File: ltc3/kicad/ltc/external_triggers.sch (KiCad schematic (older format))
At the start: 40 parts, among them P601 JST PH header, P602 JST PH housing, P605 MicroFit header, P606 MicroFit recept., P607 PowerPole, P608 PowerPole, P609 PowerPole, P610 PowerPole, P611 PowerPole, P612 PowerPole, P613 PowerPole, P614 PowerPole, Q601 PMV45EN, Q602 PMV45EN, Q603 PMV45EN, Q604 PMV45EN, SW601 SP3T, SW602 SP3T, SW603 SP3T, SW604 SP3T, U601 TLP3542, U602 TLP3542, U603 TLP3542, U604 TLP3542

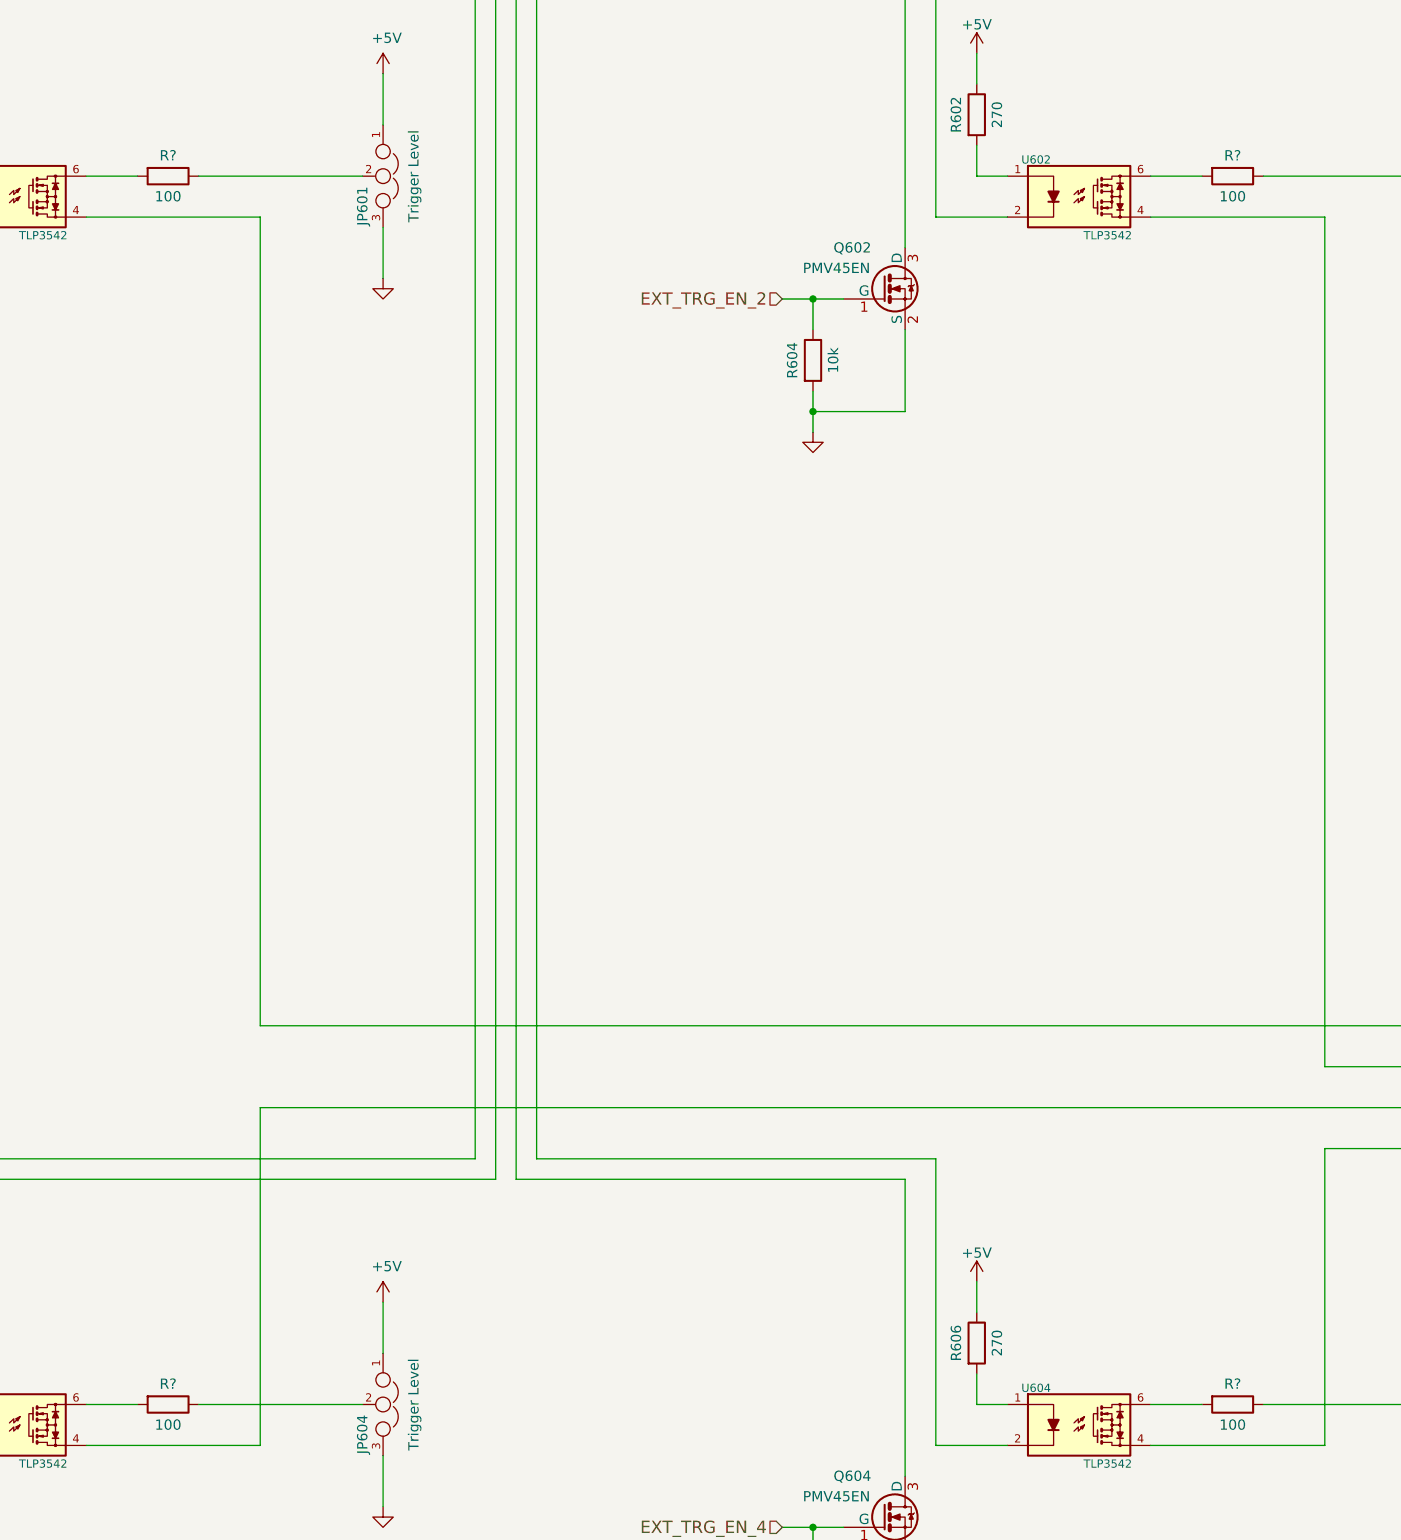
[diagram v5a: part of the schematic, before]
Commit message: LTC3: Modified LTC ignition control schematic.
Gave ignition battery ground node a distinctive symbol.
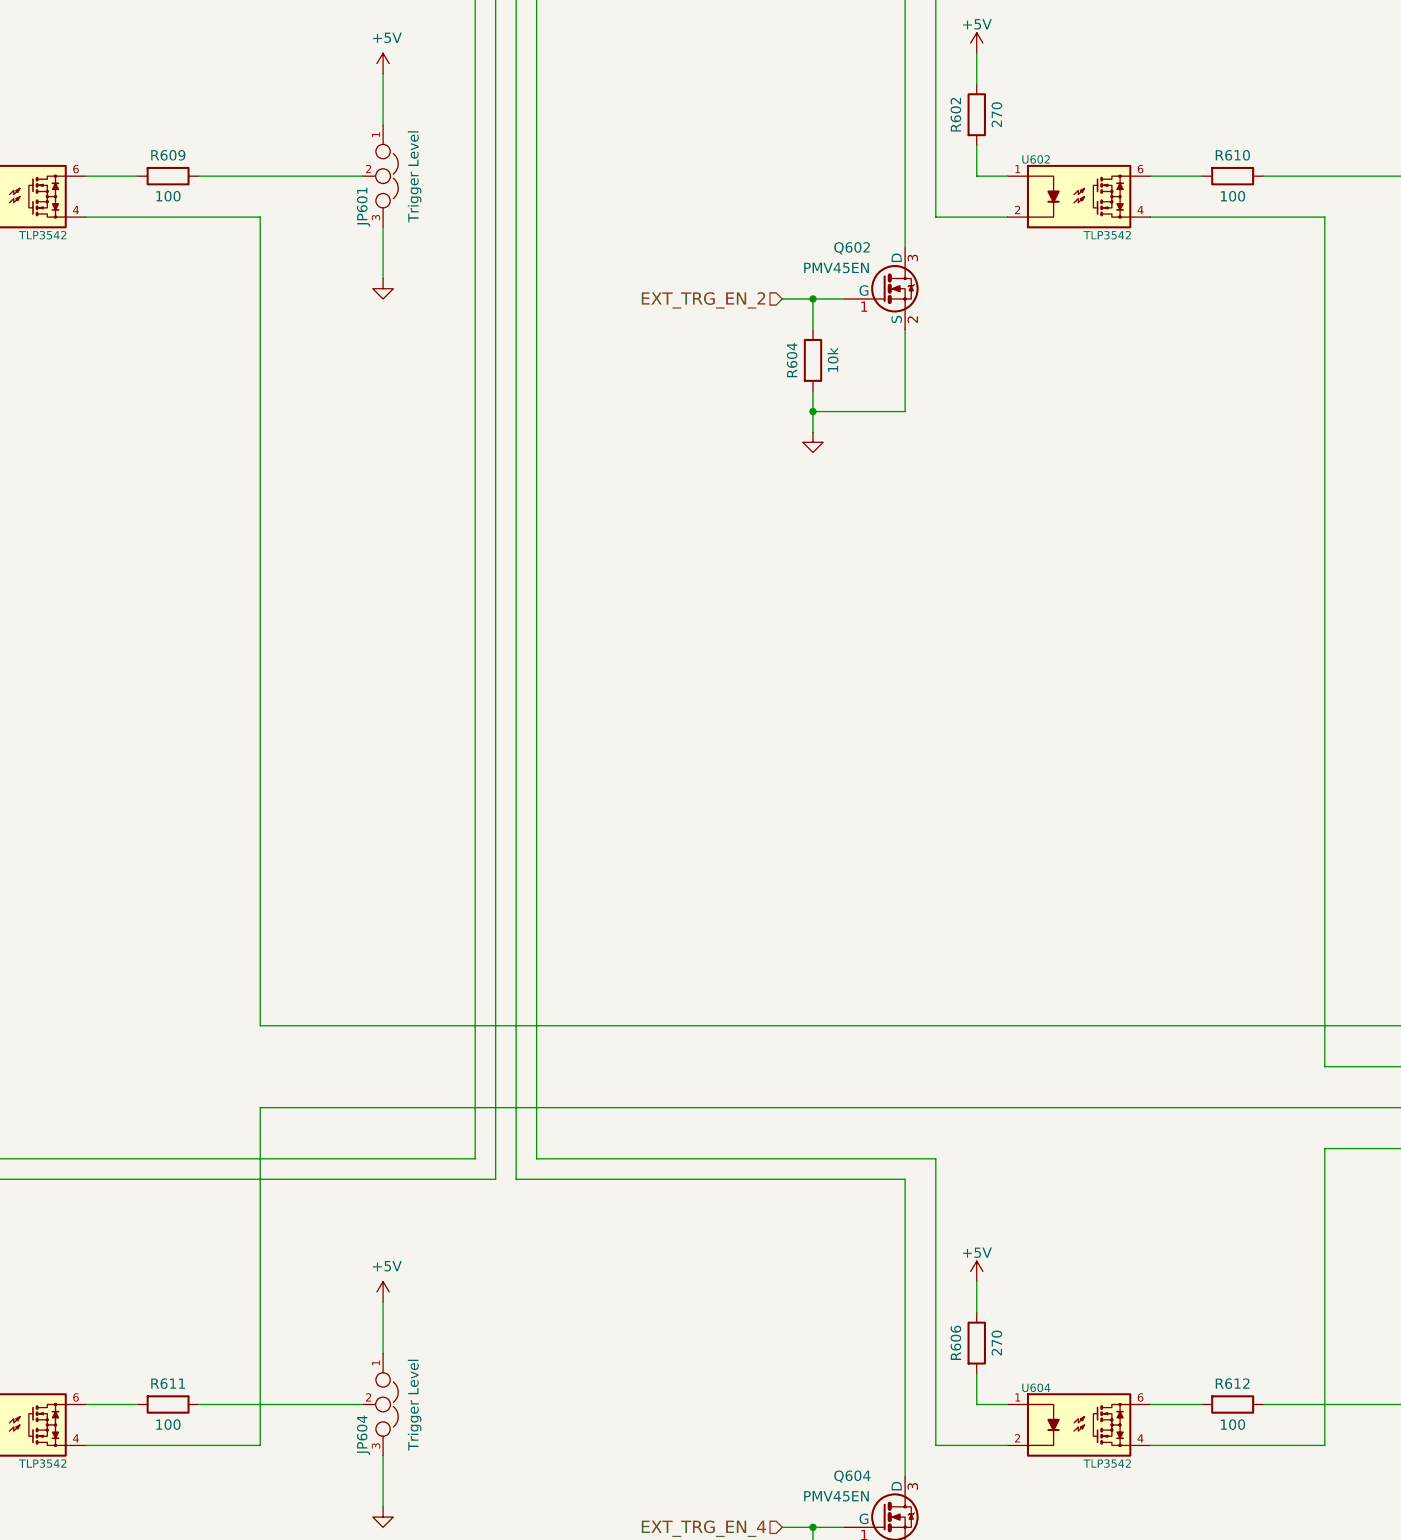
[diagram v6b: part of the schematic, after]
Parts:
- gave numbers to parts that had none: 4
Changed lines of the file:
@@
 $EndComp
 $Comp
-L GND #PWR615
+L GND #PWR616
 U 1 1 5725D3AE
 P 9850 9350
-F 0 "#PWR615" H 9850 9350 30  0001 C CNN
+F 0 "#PWR616" H 9850 9350 30  0001 C CNN
 F 1 "GND" H 9850 9280 30  0001 C CNN
 F 2 "" H 9850 9350 60  0000 C CNN
@@
 	9850 8350 9850 8600
 $Comp
-L +5V #PWR613
+L +5V #PWR614
 U 1 1 5725D3B6
 P 9850 8350
-F 0 "#PWR613" H 9850 8200 50  0001 C CNN
+F 0 "#PWR614" H 9850 8200 50  0001 C CNN
 F 1 "+5V" H 9868 8524 50  0000 C CNN
 F 2 "" H 9850 8350 50  0000 C CNN
@@
 $EndComp
 $Comp
-L GND #PWR616
+L GND #PWR615
 U 1 1 5725DD7F
 P 4750 9350
-F 0 "#PWR616" H 4750 9350 30  0001 C CNN
+F 0 "#PWR615" H 4750 9350 30  0001 C CNN
 F 1 "GND" H 4750 9280 30  0001 C CNN
 F 2 "" H 4750 9350 60  0000 C CNN
@@
 	4750 8350 4750 8600
 $Comp
-L +5V #PWR614
+L +5V #PWR613
 U 1 1 5725DD87
 P 4750 8350
-F 0 "#PWR614" H 4750 8200 50  0001 C CNN
+F 0 "#PWR613" H 4750 8200 50  0001 C CNN
 F 1 "+5V" H 4768 8524 50  0000 C CNN
 F 2 "" H 4750 8350 50  0000 C CNN
@@
 EXT_TRG_4_OUT
 $Comp
-L R R?
+L R R610
 U 1 1 57D0E30A
 P 8900 2850
-F 0 "R?" V 8800 2850 50  0000 C CNN
+F 0 "R610" V 8800 2850 50  0000 C CNN
 F 1 "100" V 9000 2850 50  0000 C CNN
 F 2 "" V 8830 2850 50  0000 C CNN
@@
 $EndComp
 $Comp
-L R R?
+L R R609
 U 1 1 57D0EA50
 P 3700 2850
-F 0 "R?" V 3600 2850 50  0000 C CNN
+F 0 "R609" V 3600 2850 50  0000 C CNN
 F 1 "100" V 3800 2850 50  0000 C CNN
 F 2 "" V 3630 2850 50  0000 C CNN
@@
 $EndComp
 $Comp
-L R R?
+L R R611
 U 1 1 57D108BE
 P 3700 8850
-F 0 "R?" V 3600 8850 50  0000 C CNN
+F 0 "R611" V 3600 8850 50  0000 C CNN
 F 1 "100" V 3800 8850 50  0000 C CNN
 F 2 "" V 3630 8850 50  0000 C CNN
@@
 $EndComp
 $Comp
-L R R?
+L R R612
 U 1 1 57D11C48
 P 8900 8850
-F 0 "R?" V 8800 8850 50  0000 C CNN
+F 0 "R612" V 8800 8850 50  0000 C CNN
 F 1 "100" V 9000 8850 50  0000 C CNN
 F 2 "" V 8830 8850 50  0000 C CNN

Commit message: LTC3: Modified LTC BeagleBone cape schematic.
Replaced external I2C connector with combined I2C/5.0V connector.
Added a second connector in parallel, so that the charge controller
and cell protection boards each have their own.
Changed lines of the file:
@@
 	2100 4000 2100 3600
 Wire Wire Line
-	1650 3900 1650 4000
-Wire Wire Line
-	1650 4000 1650 4100
+	1650 3900 1650 4100
 Wire Wire Line
 	3300 3050 4150 3050
@@
 	2450 2250 2450 2400
 Wire Wire Line
-	1500 3450 1650 3450
-Wire Wire Line
-	1650 3450 1800 3450
+	1500 3450 1800 3450
 Connection ~ 1650 3450
 Wire Wire Line
@@
 	7300 4000 7300 3600
 Wire Wire Line
-	6850 3900 6850 4000
-Wire Wire Line
-	6850 4000 6850 4100
+	6850 3900 6850 4100
 Wire Wire Line
 	8500 3050 9350 3050
@@
 	7650 2250 7650 2400
 Wire Wire Line
-	6700 3450 6850 3450
-Wire Wire Line
-	6850 3450 7000 3450
+	6700 3450 7000 3450
 Connection ~ 6850 3450
 Wire Wire Line
@@
 	2100 10000 2100 9600
 Wire Wire Line
-	1650 9900 1650 10000
-Wire Wire Line
-	1650 10000 1650 10100
+	1650 9900 1650 10100
 Wire Wire Line
 	2100 7650 2100 9200
@@
 	2450 8250 2450 8400
 Wire Wire Line
-	1500 9450 1650 9450
-Wire Wire Line
-	1650 9450 1800 9450
+	1500 9450 1800 9450
 Connection ~ 1650 9450
 Wire Wire Line
@@
 	7300 10000 7300 9600
 Wire Wire Line
-	6850 9900 6850 10000
-Wire Wire Line
-	6850 10000 6850 10100
+	6850 9900 6850 10100
 Wire Wire Line
 	7300 7750 7300 9200
@@
 	7650 8250 7650 8400
 Wire Wire Line
-	6700 9450 6850 9450
-Wire Wire Line
-	6850 9450 7000 9450
+	6700 9450 7000 9450
 Connection ~ 6850 9450
 Wire Notes Line
@@
 	13850 2600 13850 2900
 Wire Wire Line
-	13350 2900 13850 2900
-Wire Wire Line
-	13850 2900 14500 2900
-Wire Wire Line
-	14500 2900 15150 2900
-Wire Wire Line
-	15150 2900 15800 2900
+	13350 2900 15800 2900
 Wire Wire Line
 	13350 1950 13350 2900
@@
 	16200 8600 13650 8600
 Wire Wire Line
-	12850 7100 12850 7300
-Wire Wire Line
-	12850 7300 12850 7500
-Wire Wire Line
-	12850 7500 12850 7700
-Wire Wire Line
-	12850 7700 12850 7850
+	12850 7100 12850 7850
 Wire Wire Line
 	12850 7700 13000 7700

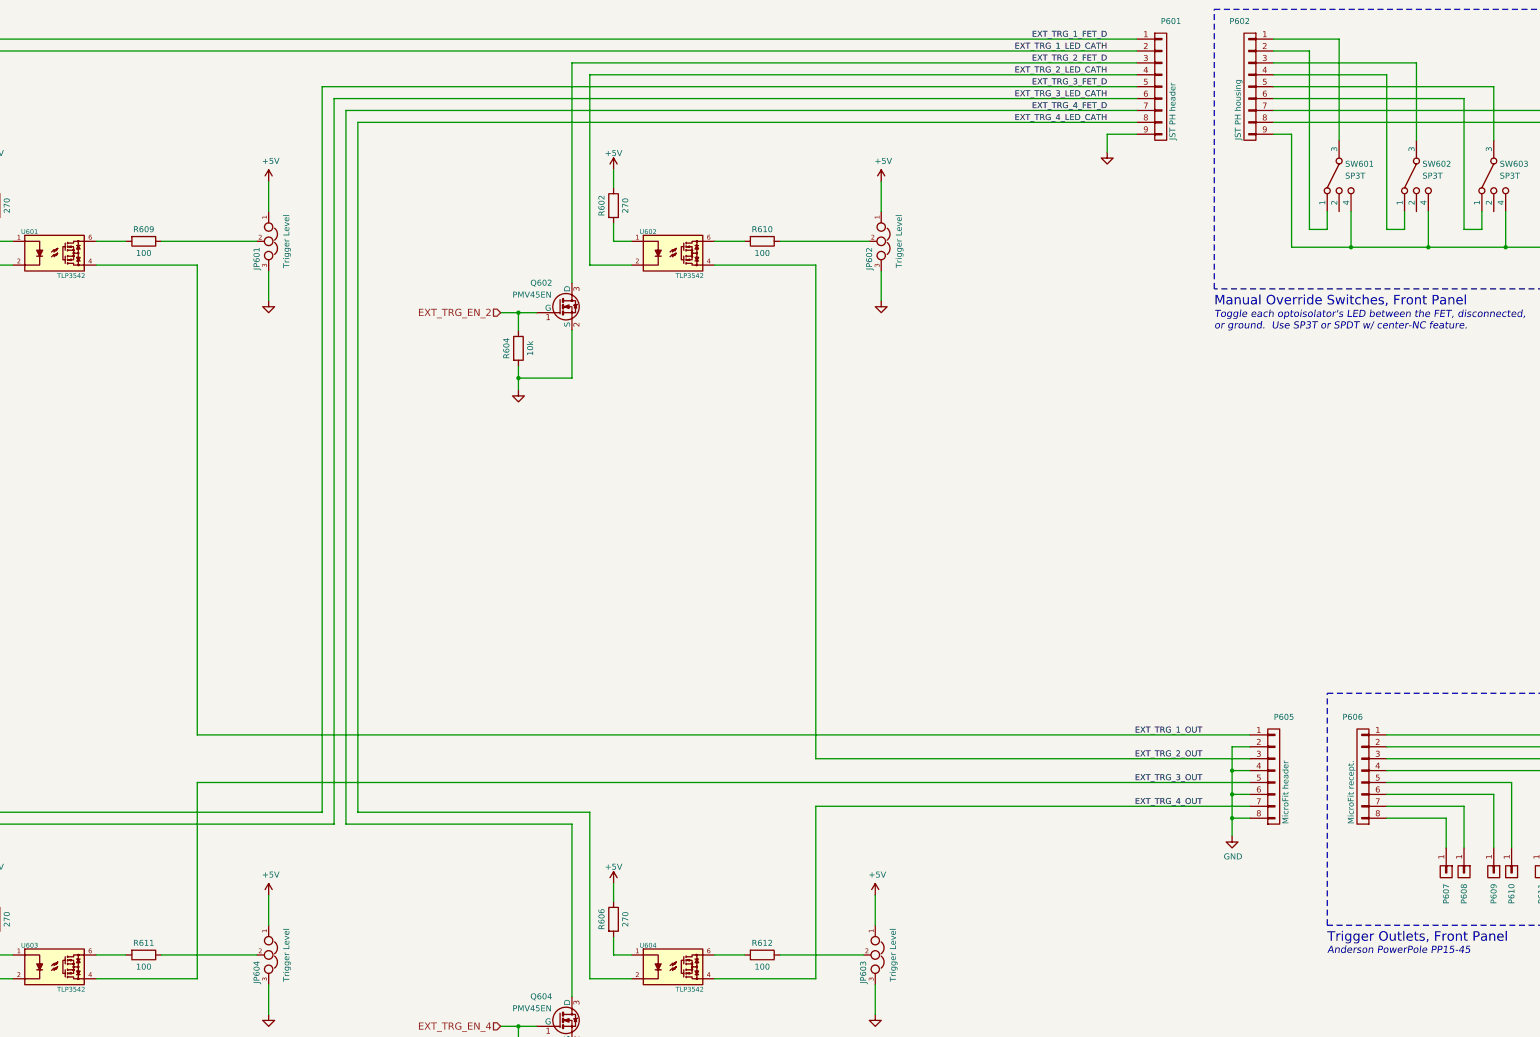
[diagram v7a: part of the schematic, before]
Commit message: LTC3: More BOM work, mostly on the LTC proper.
Plus a few minor tweaks to the charge controller and cell protection
BOMs that should not impact PCB layout.

Nearly finished with LTC BOM.
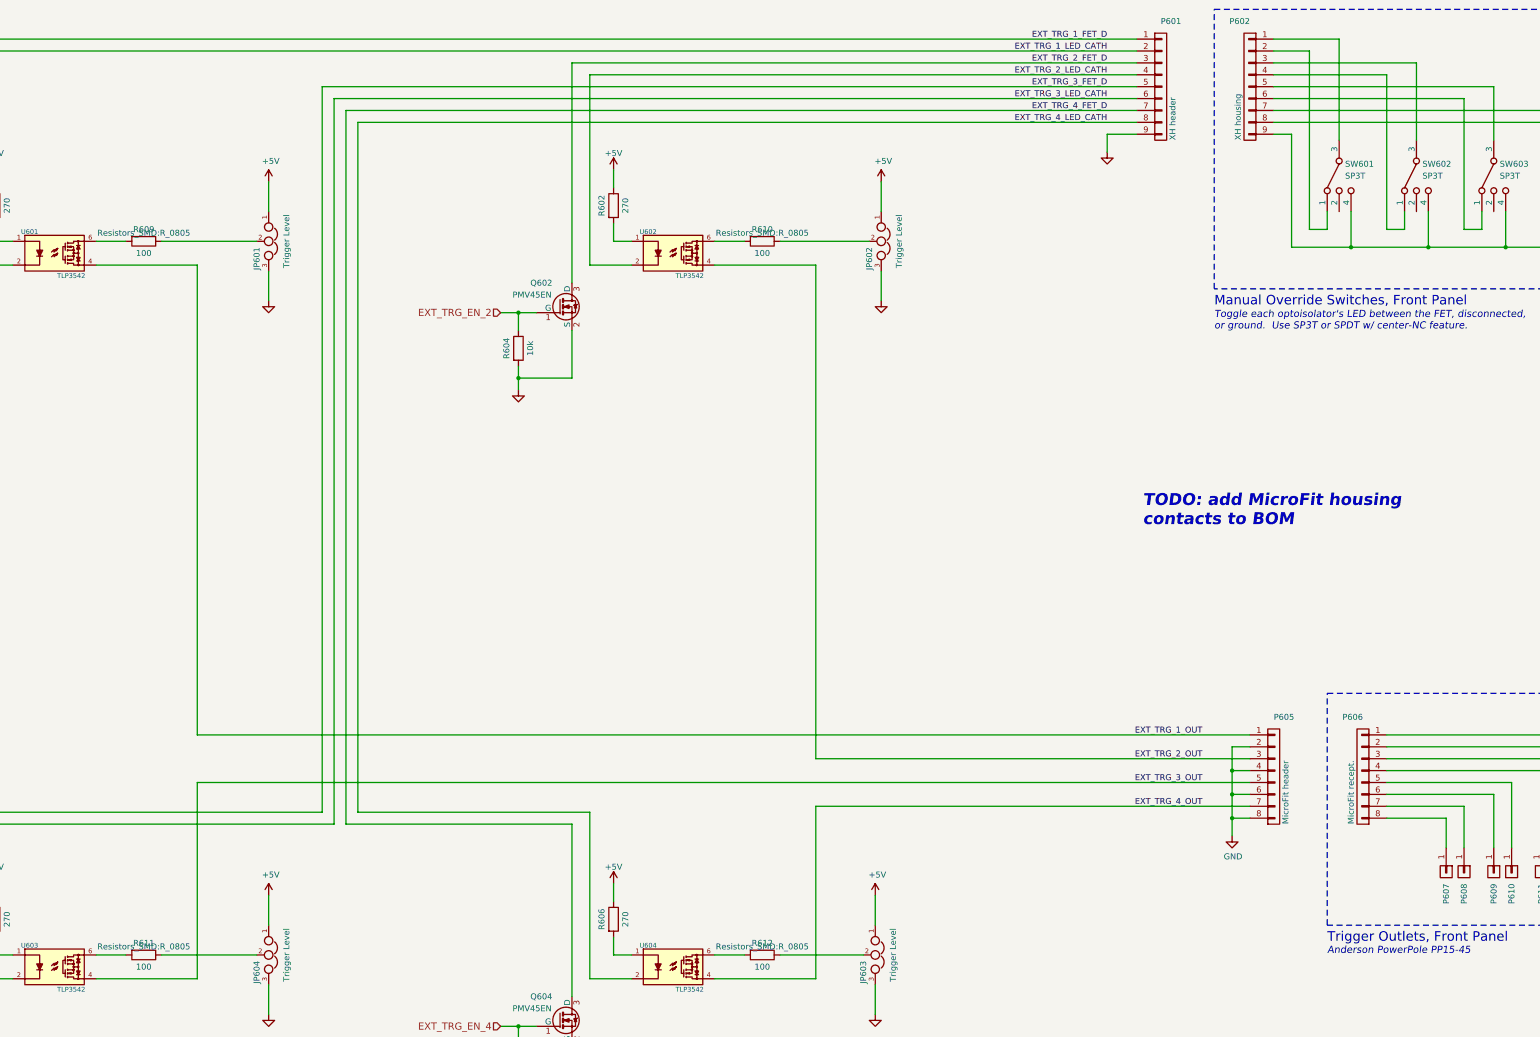
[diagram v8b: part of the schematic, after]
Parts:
- JP601, JP602, JP603, JP604: Mfg_Description (none) -> -; Mfg_Name (none) -> -; Mfg_PN (none) -> -; Note (none) -> -; Spec (none) -> -
- P601: value JST PH header -> XH header; footprint Connectors_JST:JST_PH_B9B-PH-K_09x2.00mm_Straight -> ~; Mfg_Description (none) -> -; Mfg_PN B9B-PH-K-S -> -; Note (none) -> -; Spec (none) -> -
- P602: value JST PH housing -> XH housing; footprint (none) -> ~; Mfg_Description (none) -> -; Mfg_PN PHR-9 -> -; Note (none) -> -; Spec (none) -> -
- P605: Mfg_Description (none) -> -; Spec (none) -> -
- P606, P607, P608, P609, P610, P611, P612, P613, P614: footprint (none) -> ~; Mfg_Description (none) -> -; Spec (none) -> -
- Q601, Q602, Q603, Q604: Mfg_Description (none) -> MOSFET N-CH 30V; Mfg_PN PMV45EN -> PMV45EN2R
- R601, R602, R605, R606: Mfg_Description (none) -> 1% 1/8W; Mfg_Name (none) -> Yageo; Mfg_PN (none) -> RC0805FR-07270RL; Note (none) -> -; Spec (none) -> -
- R603, R604, R607, R608: Mfg_Description (none) -> 1% 1/8W; Mfg_Name (none) -> Yageo; Mfg_PN (none) -> RC0805FR-0710KL; Note (none) -> -; Spec (none) -> -
- R609, R610, R611, R612: footprint (none) -> Resistors_SMD:R_0805; Mfg_Description (none) -> 1% 1/8W; Mfg_Name (none) -> Yageo; Mfg_PN (none) -> RC0805FR-07100RL; Note (none) -> -; Spec (none) -> -
- SW601, SW602, SW603, SW604: footprint (none) -> ~; Mfg_Description (none) -> -; Mfg_Name (none) -> -; Mfg_PN (none) -> -; Note (none) -> OFF-BOARD; Spec (none) -> -
- U601, U602, U603, U604: Mfg_Description (none) -> -
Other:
- note added: "TODO: add MicroFit housing\ncontacts to BOM"
